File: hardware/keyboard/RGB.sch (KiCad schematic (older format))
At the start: 28 parts, among them U2 IS31FL3733-QF, U3 IS31FL3733-QF

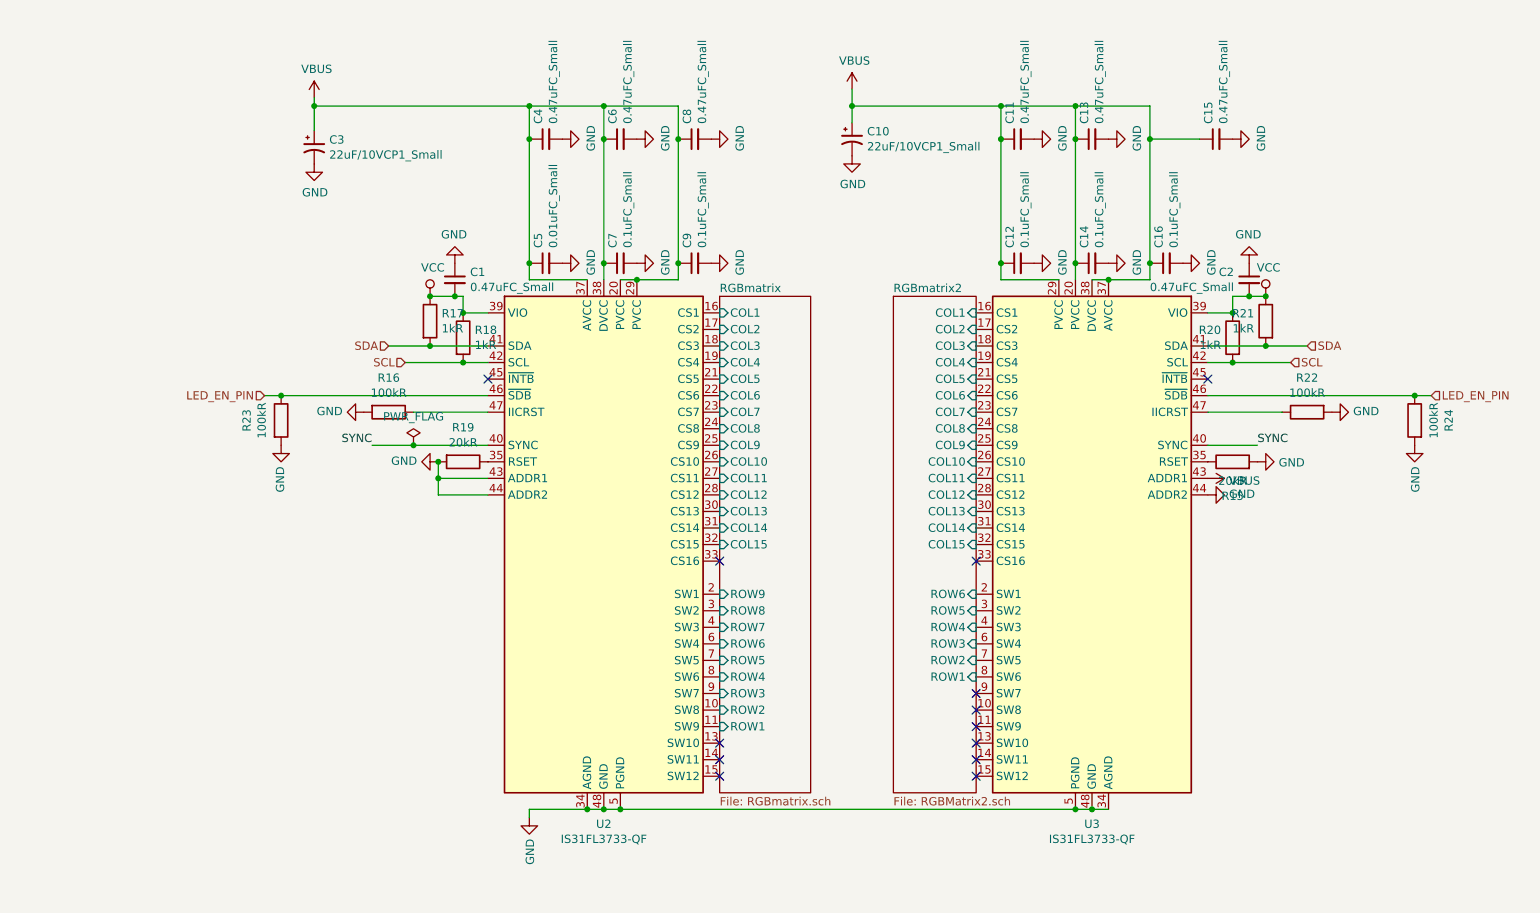
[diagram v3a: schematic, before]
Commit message: use proper footprint, link symbols and footprints
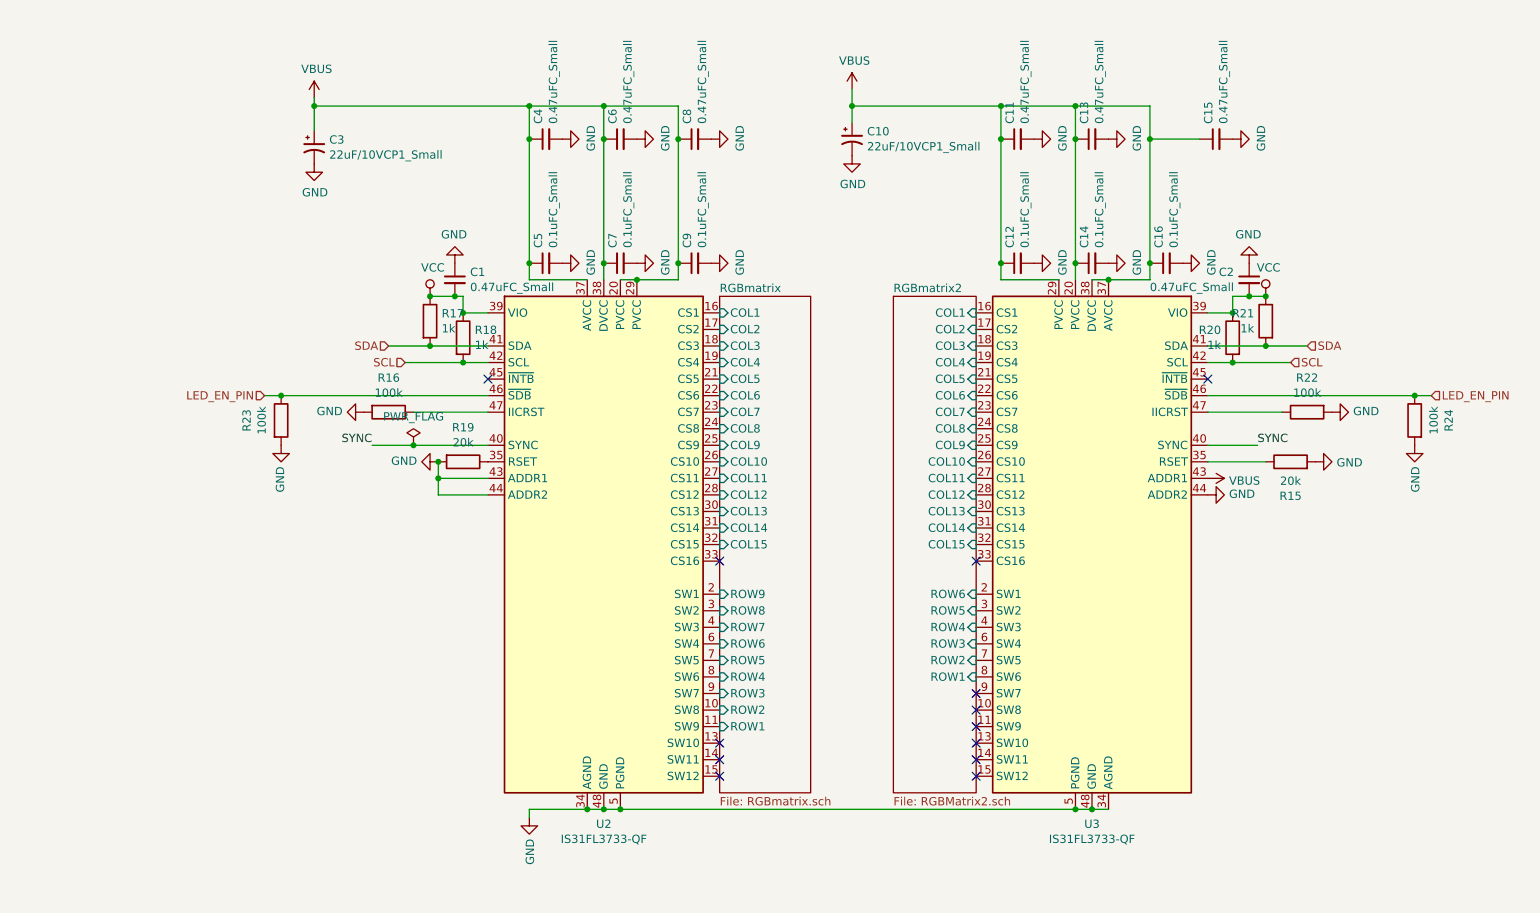
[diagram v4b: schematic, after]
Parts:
- C1, C11, C13, C15, C2, C4, C6, C8: footprint (none) -> Capacitor_SMD:C_0603_1608Metric_Pad1.05x0.95mm_HandSolder; Footprint (none) -> Capacitor_SMD:C_0603_1608Metric_Pad1.05x0.95mm_HandSolder; Value (none) -> 0.47μF
- C10, C3: footprint (none) -> Capacitor_Tantalum_SMD:CP_EIA-3528-12_Kemet-T_Pad1.50x2.35mm_HandSolder; Footprint (none) -> Capacitor_Tantalum_SMD:CP_EIA-3528-12_Kemet-T_Pad1.50x2.35m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; Value (none) -> 22μF/10V
- C12, C14, C16, C7, C9: footprint (none) -> Capacitor_SMD:C_0603_1608Metric_Pad1.05x0.95mm_HandSolder; Footprint (none) -> Capacitor_SMD:C_0603_1608Metric_Pad1.05x0.95mm_HandSolder; Value (none) -> 0.1μF
- C5: value 0.01uFC_Small -> 0.1uFC_Small; footprint (none) -> Capacitor_SMD:C_0603_1608Metric_Pad1.05x0.95mm_HandSolder; Footprint (none) -> Capacitor_SMD:C_0603_1608Metric_Pad1.05x0.95mm_HandSolder; Value (none) -> 0.1μF
- R15, R19: value 20kR -> 20k; footprint (none) -> Resistor_SMD:R_0603_1608Metric_Pad1.05x0.95mm_HandSolder; Footprint (none) -> Resistor_SMD:R_0603_1608Metric_Pad1.05x0.95mm_HandSolder; Value (none) -> 20k
- R16, R22, R23, R24: value 100kR -> 100k; footprint (none) -> Resistor_SMD:R_0603_1608Metric_Pad1.05x0.95mm_HandSolder; Footprint (none) -> Resistor_SMD:R_0603_1608Metric_Pad1.05x0.95mm_HandSolder; Value (none) -> 100k
- R17, R18, R20, R21: value 1kR -> 1k; footprint (none) -> Resistor_SMD:R_0603_1608Metric_Pad1.05x0.95mm_HandSolder; Footprint (none) -> Resistor_SMD:R_0603_1608Metric_Pad1.05x0.95mm_HandSolder; Value (none) -> 1k
- U2, U3: footprint Package_DFN_QFN:QFN-48-1EP_6x6mm_P0.4mm_EP4.2x4.2mm -> Package_DFN_QFN:QFN-48-1EP_6x6mm_P0.4mm_EP4.2x4.2mm_ThermalVias; Footprint (none) -> Package_DFN_QFN:QFN-48-1EP_6x6mm_P0.4mm_EP4.2x4.2mm_Thermal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; Value (none) -> IS31FL7377
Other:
- moved on the sheet: R15

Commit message: make everything cleaner
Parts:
- C1, C11, C13, C15, C2, C4, C6, C8: value 0.47uFC_Small -> 0.47μF
- C10, C3: value 22uF/10VCP1_Small -> 22μF/10V
- C12, C14, C16, C5, C7, C9: value 0.1uFC_Small -> 0.1μF
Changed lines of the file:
@@
 P 8050 2000
 F 0 "C2" H 8142 2046 50  0000 L CNN
-F 1 "0.47uFC_Small" H 8142 1955 50  0000 L CNN
+F 1 "0.47μF" H 8142 1955 50  0000 L CNN
 F 2 "Capacitor_SMD:C_0603_1608Metric_Pad1.05x0.95mm_HandSolder" H 8050 2000 50  0001 C CNN
 F 3 "~" H 8050 2000 50  0001 C CNN
@@
 P 3250 2000
 F 0 "C1" H 3342 2046 50  0000 L CNN
-F 1 "0.47uFC_Small" H 3342 1955 50  0000 L CNN
+F 1 "0.47μF" H 3342 1955 50  0000 L CNN
 F 2 "Capacitor_SMD:C_0603_1608Metric_Pad1.05x0.95mm_HandSolder" H 3250 2000 50  0001 C CNN
 F 3 "~" H 3250 2000 50  0001 C CNN
@@
 P 7100 1900
 F 0 "C14" H 7192 1946 50  0000 L CNN
-F 1 "0.1uFC_Small" H 7192 1855 50  0000 L CNN
+F 1 "0.1μF" H 7192 1855 50  0000 L CNN
 F 2 "Capacitor_SMD:C_0603_1608Metric_Pad1.05x0.95mm_HandSolder" H 7100 1900 50  0001 C CNN
 F 3 "~" H 7100 1900 50  0001 C CNN
@@
 P 7100 1150
 F 0 "C13" H 7192 1196 50  0000 L CNN
-F 1 "0.47uFC_Small" H 7192 1105 50  0000 L CNN
+F 1 "0.47μF" H 7192 1105 50  0000 L CNN
 F 2 "Capacitor_SMD:C_0603_1608Metric_Pad1.05x0.95mm_HandSolder" H 7100 1150 50  0001 C CNN
 F 3 "~" H 7100 1150 50  0001 C CNN
@@
 P 6650 1900
 F 0 "C12" H 6742 1946 50  0000 L CNN
-F 1 "0.1uFC_Small" H 6742 1855 50  0000 L CNN
+F 1 "0.1μF" H 6742 1855 50  0000 L CNN
 F 2 "Capacitor_SMD:C_0603_1608Metric_Pad1.05x0.95mm_HandSolder" H 6650 1900 50  0001 C CNN
 F 3 "~" H 6650 1900 50  0001 C CNN
@@
 P 6650 1150
 F 0 "C11" H 6742 1196 50  0000 L CNN
-F 1 "0.47uFC_Small" H 6742 1105 50  0000 L CNN
+F 1 "0.47μF" H 6742 1105 50  0000 L CNN
 F 2 "Capacitor_SMD:C_0603_1608Metric_Pad1.05x0.95mm_HandSolder" H 6650 1150 50  0001 C CNN
 F 3 "~" H 6650 1150 50  0001 C CNN
@@
 P 7550 1900
 F 0 "C16" H 7642 1946 50  0000 L CNN
-F 1 "0.1uFC_Small" H 7642 1855 50  0000 L CNN
+F 1 "0.1μF" H 7642 1855 50  0000 L CNN
 F 2 "Capacitor_SMD:C_0603_1608Metric_Pad1.05x0.95mm_HandSolder" H 7550 1900 50  0001 C CNN
 F 3 "~" H 7550 1900 50  0001 C CNN
@@
 P 7850 1150
 F 0 "C15" H 7942 1196 50  0000 L CNN
-F 1 "0.47uFC_Small" H 7942 1105 50  0000 L CNN
+F 1 "0.47μF" H 7942 1105 50  0000 L CNN
 F 2 "Capacitor_SMD:C_0603_1608Metric_Pad1.05x0.95mm_HandSolder" H 7850 1150 50  0001 C CNN
 F 3 "~" H 7850 1150 50  0001 C CNN
@@
 P 5650 1150
 F 0 "C10" H 5741 1196 50  0000 L CNN
-F 1 "22uF/10VCP1_Small" H 5741 1105 50  0000 L CNN
+F 1 "22μF/10V" H 5741 1105 50  0000 L CNN
 F 2 "Capacitor_Tantalum_SMD:CP_EIA-3528-12_Kemet-T_Pad1.50x2.35mm_HandSolder" H 5650 1150 50  0001 C CNN
 F 3 "~" H 5650 1150 50  0001 C CNN
@@
 P 4250 1900
 F 0 "C7" H 4342 1946 50  0000 L CNN
-F 1 "0.1uFC_Small" H 4342 1855 50  0000 L CNN
+F 1 "0.1μF" H 4342 1855 50  0000 L CNN
 F 2 "Capacitor_SMD:C_0603_1608Metric_Pad1.05x0.95mm_HandSolder" H 4250 1900 50  0001 C CNN
 F 3 "~" H 4250 1900 50  0001 C CNN
@@
 P 4250 1150
 F 0 "C6" H 4342 1196 50  0000 L CNN
-F 1 "0.47uFC_Small" H 4342 1105 50  0000 L CNN
+F 1 "0.47μF" H 4342 1105 50  0000 L CNN
 F 2 "Capacitor_SMD:C_0603_1608Metric_Pad1.05x0.95mm_HandSolder" H 4250 1150 50  0001 C CNN
 F 3 "~" H 4250 1150 50  0001 C CNN
@@
 P 3800 1900
 F 0 "C5" H 3892 1946 50  0000 L CNN
-F 1 "0.1uFC_Small" H 3892 1855 50  0000 L CNN
+F 1 "0.1μF" H 3892 1855 50  0000 L CNN
 F 2 "Capacitor_SMD:C_0603_1608Metric_Pad1.05x0.95mm_HandSolder" H 3800 1900 50  0001 C CNN
 F 3 "~" H 3800 1900 50  0001 C CNN
@@
 P 3800 1150
 F 0 "C4" H 3892 1196 50  0000 L CNN
-F 1 "0.47uFC_Small" H 3892 1105 50  0000 L CNN
+F 1 "0.47μF" H 3892 1105 50  0000 L CNN
 F 2 "Capacitor_SMD:C_0603_1608Metric_Pad1.05x0.95mm_HandSolder" H 3800 1150 50  0001 C CNN
 F 3 "~" H 3800 1150 50  0001 C CNN
@@
 P 4700 1900
 F 0 "C9" H 4792 1946 50  0000 L CNN
-F 1 "0.1uFC_Small" H 4792 1855 50  0000 L CNN
+F 1 "0.1μF" H 4792 1855 50  0000 L CNN
 F 2 "Capacitor_SMD:C_0603_1608Metric_Pad1.05x0.95mm_HandSolder" H 4700 1900 50  0001 C CNN
 F 3 "~" H 4700 1900 50  0001 C CNN
@@
 P 4700 1150
 F 0 "C8" H 4792 1196 50  0000 L CNN
-F 1 "0.47uFC_Small" H 4792 1105 50  0000 L CNN
+F 1 "0.47μF" H 4792 1105 50  0000 L CNN
 F 2 "Capacitor_SMD:C_0603_1608Metric_Pad1.05x0.95mm_HandSolder" H 4700 1150 50  0001 C CNN
 F 3 "~" H 4700 1150 50  0001 C CNN
@@
 P 2400 1200
 F 0 "C3" H 2491 1246 50  0000 L CNN
-F 1 "22uF/10VCP1_Small" H 2491 1155 50  0000 L CNN
+F 1 "22μF/10V" H 2491 1155 50  0000 L CNN
 F 2 "Capacitor_Tantalum_SMD:CP_EIA-3528-12_Kemet-T_Pad1.50x2.35mm_HandSolder" H 2400 1200 50  0001 C CNN
 F 3 "~" H 2400 1200 50  0001 C CNN
